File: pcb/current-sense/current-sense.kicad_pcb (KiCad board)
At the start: 4 copper layers, 130 x 25 mm, 113 parts, among them J1 M3, J2 M3, J3 Tag Connect, J4 M3, J5 M3, J6 Conn_Coaxial, J7 AA Holder, J8 DNP, Q1 FDC6327C, SW1 SW_Push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

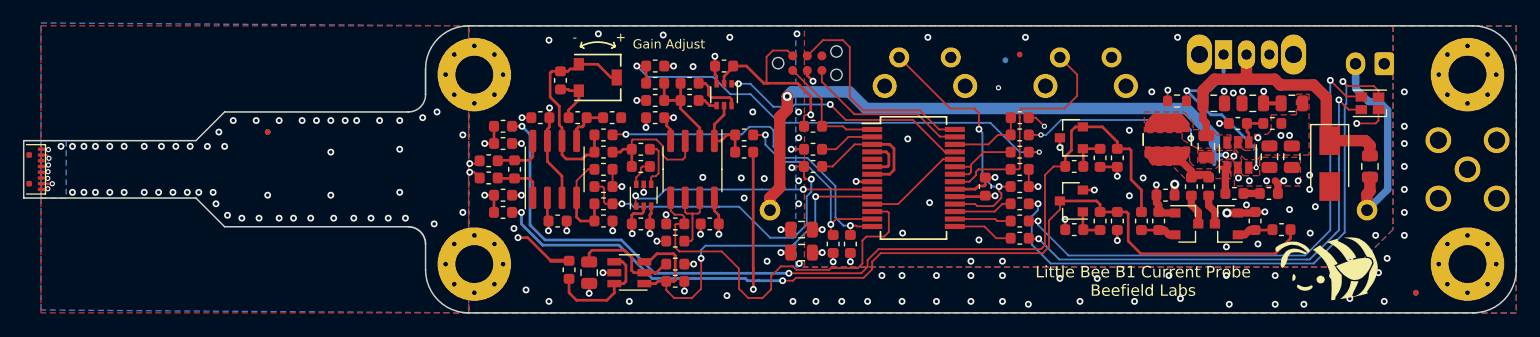
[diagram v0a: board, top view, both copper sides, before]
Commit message: enlarge via to 0.3mm
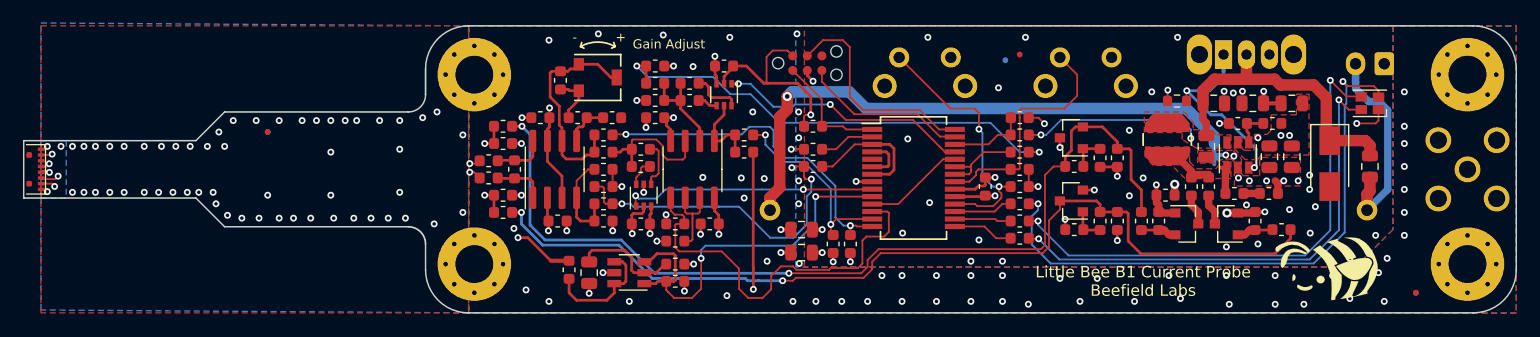
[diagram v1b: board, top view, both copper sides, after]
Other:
- net class Default removed
